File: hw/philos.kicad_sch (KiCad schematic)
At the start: 21 parts, among them SW1 Reset Button, U1 8086_Min_Mode, U10 MAX232N, U11 W27C512-45Z, U12 71256SA25TPGI, U2 SN74LS373N, U3 SN74LS373N, U4 SN74LS373N, U5 W27C512-45Z, U7 71256SA25TPGI, U8 SN74LS161AN, U9 SN74AHC14N, Y1 Crystal 15 MHz

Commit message: hw: add 8255 and 8259
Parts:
- added R4: 10K ohm, symbol Device:R
- added U13: 8259, Package_DIP:DIP-28_W15.24mm, symbol Interface:8259
- added U14: 8255, Package_DIP:DIP-40_W15.24mm, symbol Interface:8255
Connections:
- net GND: now also U13.14 (GND), U14.35 (RESET), U14.7 (GND); no longer U1.18 (INTR)
- net VCC: now also R4.2, U13.28 (VCC), U14.26 (VCC)
- net dati0: now also U13.11 (D0), U14.34 (D0)
- net dati1: now also U13.10 (D1), U14.33 (D1)
- net dati2: now also U13.9 (D2), U14.32 (D2)
- net dati3: now also U13.8 (D3), U14.31 (D3)
- net dati4: now also U13.7 (D4), U14.30 (D4)
- net dati5: now also U13.6 (D5), U14.29 (D5)
- net dati6: now also U13.5 (D6), U14.28 (D6)
- net dati7: now also U13.4 (D7), U14.27 (D7)
- net indirizzi18: now also U14.9 (A0)
- net indirizzi19: now also U13.27 (A0), U14.8 (A1)
- net at U1.32 (~{RD}), U12.22 (~{OE}), U6.13 (*RD)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: now also U13.3 (~{RD}), U14.5 (~{RD})
- net at U1.29 (~{WR}), U12.27 (~{WE}), U6.10 (*WR)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: now also U13.2 (~{WR}), U14.36 (~{WR})
- net at U1.24 (~{INTA}): now also U13.26 (~{INTA})
- new net: R4.1, U13.16 (~{SP}/~{EN})
- new net: U1.18 (INTR), U13.17 (INT)

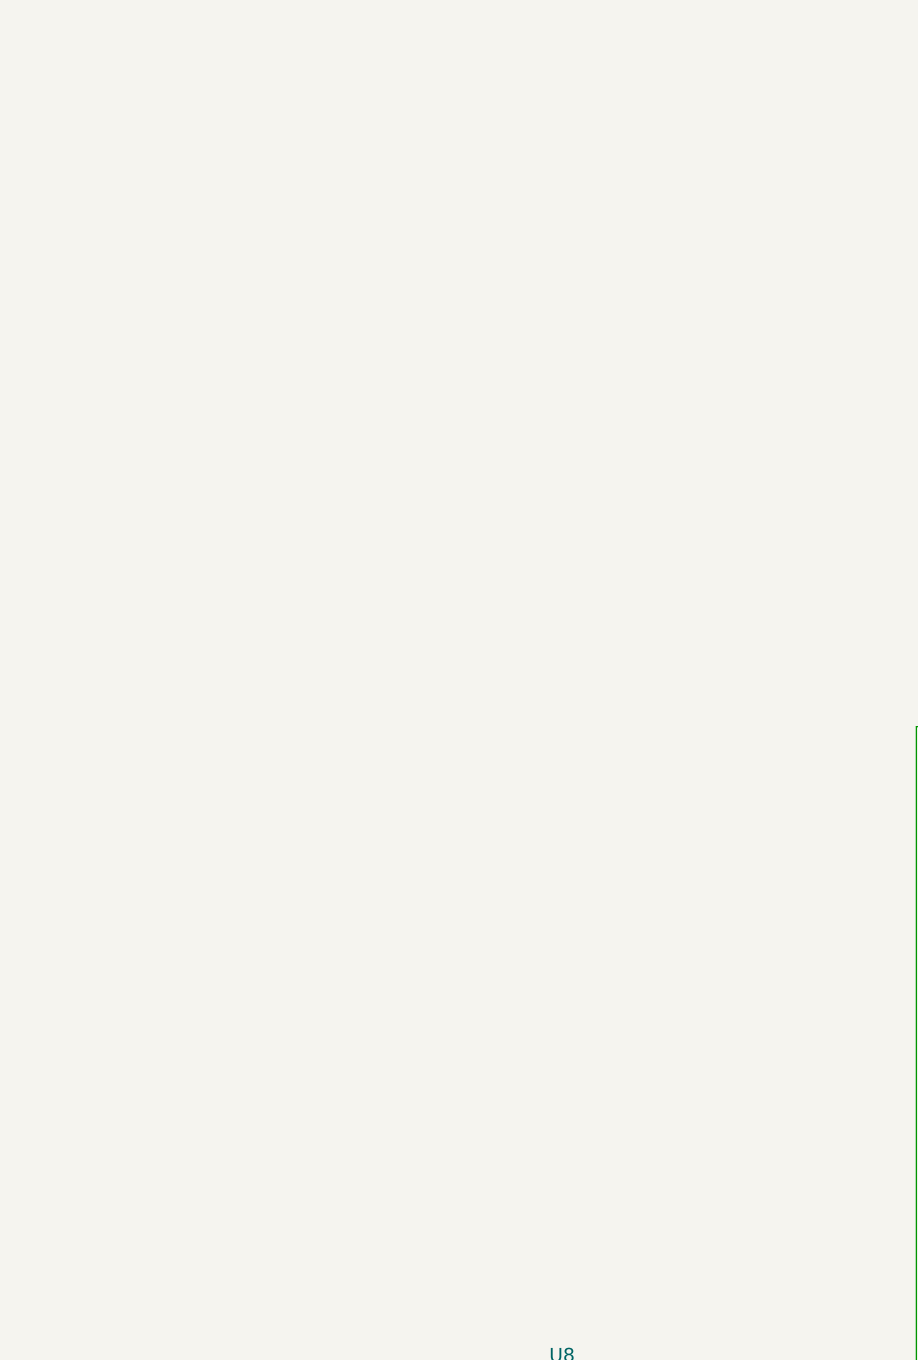
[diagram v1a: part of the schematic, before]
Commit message: hw: Add Arduino Mega
Signed-off-by: Matteo Bertolino <m.bertolino.m@gmail.com>
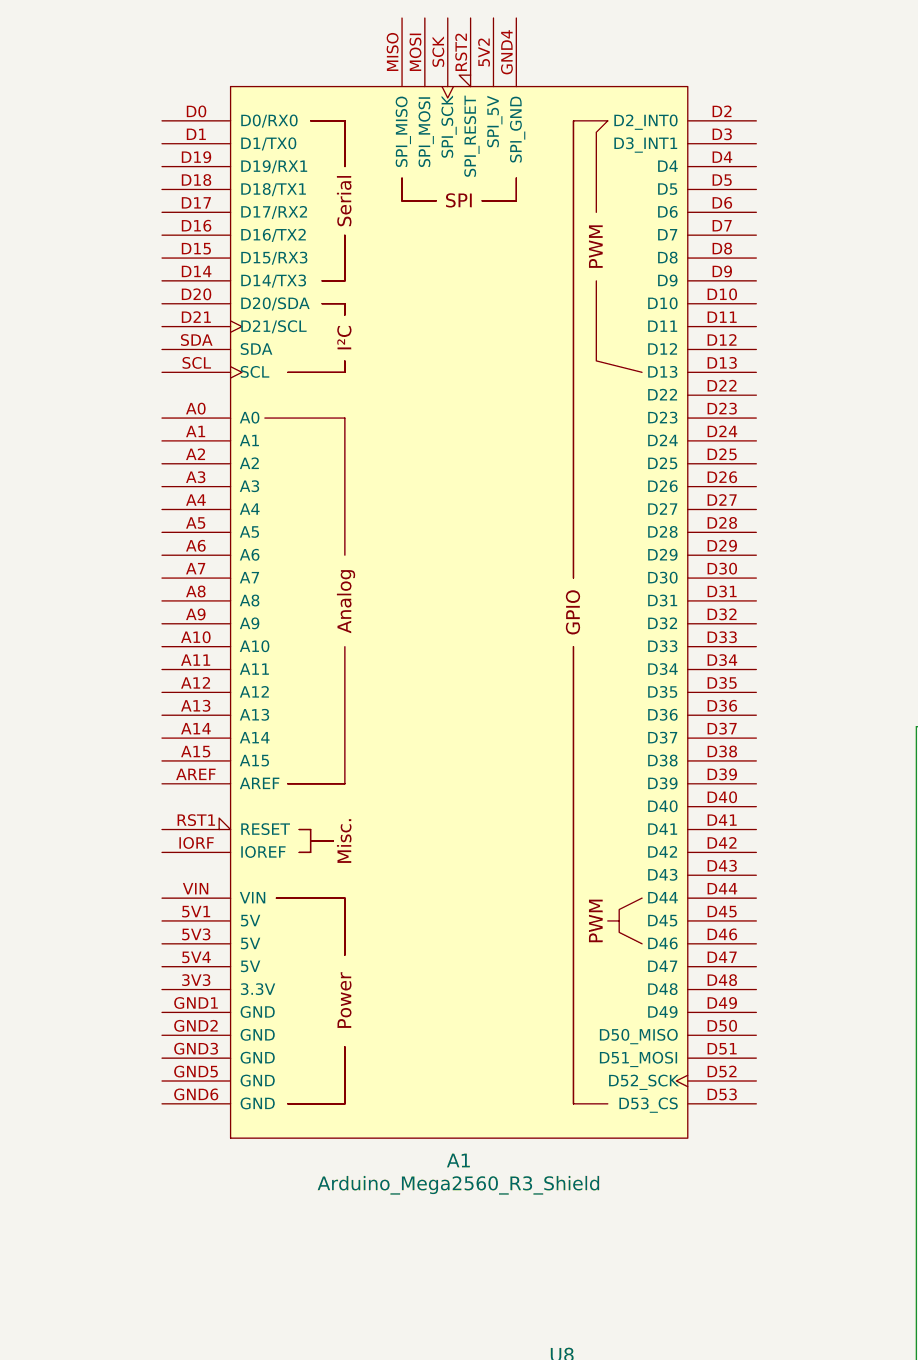
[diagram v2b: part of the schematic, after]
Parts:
- added A1: Arduino_Mega2560_R3_Shield, PCM_arduino-library:Arduino_Mega2560_R3_Shield, symbol Arduino:Arduino_Mega2560_R3_Shield

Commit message: docs: Add DFD prototype
Signed-off-by: Matteo Bertolino <m.bertolino.m@gmail.com>
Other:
- note added: "philOS"
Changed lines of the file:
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@@
 	(title_block
 		(title "philOS")
-		(date "2025-02-26")
+		(date "2025-03-07")
 		(rev "0")
 	)
+	(text "philOS"
+		(exclude_from_sim no)
+		(at 528.574 385.318 0)
+		(effects
+			(font
+				(face "Jersey 25")
+				(size 12 12)
+				(bold yes)
+				(color 0 0 0 1)
+			)
+		)
+	)
 	(junction
 		(at 92.71 200.66)
@@
 		)
 	)
-	(label "A19 1 = comando 0 = dato"
+	(label "A19: 1 = comando, 0 = dato"
 		(at 325.12 340.36 0)
 		(effects

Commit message: hw: manage the chip select pins
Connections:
- net indirizzi0: now also A1.D2 (D2_INT0)
- net indirizzi1: now also A1.D3 (D3_INT1)
- net indirizzi10: now also A1.D12
- net indirizzi11: now also A1.D13
- net indirizzi12: now also A1.D22
- net indirizzi13: now also A1.D23
- net indirizzi14: now also A1.D24
- net indirizzi15: now also A1.D25
- net indirizzi16: now also A1.D26
- net indirizzi17: now also A1.D27
- net indirizzi18: now also A1.D28
- net indirizzi19: now also A1.D29
- net indirizzi2: now also A1.D4
- net indirizzi3: now also A1.D5
- net indirizzi4: now also A1.D6
- net indirizzi5: now also A1.D7
- net indirizzi6: now also A1.D8
- net indirizzi7: now also A1.D9
- net indirizzi8: now also A1.D10
- net indirizzi9: now also A1.D11
- net at U5.20 (*CE): now also A1.D37
- net at U14.6 (~{CS}): now also A1.D33
- net at U7.20 (~{CS}): now also A1.D35, U12.20 (~{CS})
- net at U11.20 (*CE): now also A1.D36
- net at U1.28 (M/~{IO}): now also A1.D30
- net at DS1.8 (E): now also A1.D32
- net at A1.D31: now also U6.11 (*CS)
- net at A1.D34: now also U13.1 (~{CS})

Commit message: hw: improve the schematic
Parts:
- removed A1: Arduino_Mega2560_R3_Shield, PCM_arduino-library:Arduino_Mega2560_R3_Shield, symbol Arduino:Arduino_Mega2560_R3_Shield
- removed C1, C2: 15pF, K150J15C0GF5TL2_VIS, symbol K150J15C0GF5TL2:K150J15C0GF5TL2
- removed R1: 270 ohm, symbol Device:R
- removed R2: 1M ohm, symbol Device:R
- removed U10: MAX232N, N16, symbol MAX232N:MAX232N
- removed U11: W27C512-45Z, 28P-DIP, symbol W27C512-45Z:W27C512-45Z
- removed U12, U7: 71256SA25TPGI, 71256SA25TPGI:DIP787W47P254L3467H457Q28B, symbol 71256SA25TPGI:71256SA25TPGI
- removed U13: 8259, Package_DIP:DIP-28_W15.24mm, symbol Interface:8259
- removed U14: 8255, Package_DIP:DIP-40_W15.24mm, symbol Interface:8255
- removed U6: ~, symbol P8251A:P8251A
- removed U8: SN74LS161AN, N16, symbol SN74LS161AN:SN74LS161AN
- removed U9: SN74AHC14N, N14, symbol SN74AHC14N:SN74AHC14N
- removed Y1: Crystal 15 MHz, symbol Device:Crystal
- added A2: Arduino_Mega2560_R3_Shield, PCM_arduino-library:Arduino_Mega2560_R3_Shield, symbol Arduino:Arduino_Mega2560_R3_Shield
- added C3, C4: 15pF, K150J15C0GF5TL2_VIS, symbol K150J15C0GF5TL2:K150J15C0GF5TL2
- added R5: 10K ohm, symbol Device:R
- added R7: 270 ohm, symbol Device:R
- added U11, U16: 71256SA25TPGI, 71256SA25TPGI:DIP787W47P254L3467H457Q28B, symbol 71256SA25TPGI:71256SA25TPGI
- added U12: SN74LS161AN, N16, symbol SN74LS161AN:SN74LS161AN
- added U13: SN74AHC14N, N14, symbol SN74AHC14N:SN74AHC14N
- added U14: 8259, Package_DIP:DIP-28_W15.24mm, symbol Interface:8259
- added U15: W27C512-45Z, 28P-DIP, symbol W27C512-45Z:W27C512-45Z
- added U17: 8255, Package_DIP:DIP-40_W15.24mm, symbol Interface:8255
- added U18: MAX232N, N16, symbol MAX232N:MAX232N
- added U7: ~, symbol P8251A:P8251A
- added Y2: Crystal 15 MHz, symbol Device:Crystal
- R4: value 10K ohm -> 1M ohm
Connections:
- net GND: now also C3.2, C4.2, U11.14 (GND), U12.3 (A), U12.4 (B), U12.5 (C), U12.6 (D), U12.8 (GND), U13.7 (GND), U14.14 (GND), U15.14 (GND), U15.22 (*OE/VPP), U16.14 (GND), U17.35 (RESET), U17.7 (GND), U18.15 (GND), U18.2 (Vs+), U18.6 (Vs-), U7.17 (*CTS), U7.21 (reset), U7.22 (*DSR), U7.4 (GND)
- net VCC: now also R5.2, U11.28 (VCC), U12.1 (*CLR), U12.10 (ENT), U12.16 (VCC), U12.7 (ENP), U12.9 (*LOAD), U13.14 (VCC), U14.28 (VCC), U15.28 (VCC), U16.28 (VCC), U17.26 (VCC), U18.16 (VCC), U7.23 (*RTS), U7.26 (Vcc); no longer R4.2
- net dati0: now also U11.11 (I/O0), U14.11 (D0), U15.11 (Q0), U17.34 (D0), U7.27 (D0)
- net dati1: now also U11.12 (I/O1), U14.10 (D1), U15.12 (Q1), U17.33 (D1), U7.28 (D1)
- net dati10: now also U16.13 (I/O2)
- net dati11: now also U16.15 (I/O3)
- net dati12: now also U16.16 (I/O4)
- net dati13: now also U16.17 (I/O5)
- net dati14: now also U16.18 (I/O6)
- net dati15: now also U16.19 (I/O7)
- net dati2: now also U11.13 (I/O2), U14.9 (D2), U15.13 (Q2), U17.32 (D2), U7.1 (D2)
- net dati3: now also U11.15 (I/O3), U14.8 (D3), U15.15 (Q3), U17.31 (D3), U7.2 (D3)
- net dati4: now also U11.16 (I/O4), U14.7 (D4), U15.16 (Q4), U17.30 (D4), U7.5 (D4)
- net dati5: now also U11.17 (I/O5), U14.6 (D5), U15.17 (Q5), U17.29 (D5), U7.6 (D5)
- net dati6: now also U11.18 (I/O6), U14.5 (D6), U15.18 (Q6), U17.28 (D6), U7.7 (D6)
- net dati7: now also U11.19 (I/O7), U14.4 (D7), U15.19 (Q7), U17.27 (D7), U7.8 (D7)
- net dati8: now also U16.11 (I/O0)
- net dati9: now also U16.12 (I/O1)
- net indirizzi0: now also A2.D2 (D2_INT0), U11.10 (A0), U15.10 (A0), U16.10 (A0)
- net indirizzi1: now also A2.D3 (D3_INT1), U11.9 (A1), U15.9 (A1), U16.9 (A1)
- net indirizzi10: now also A2.D12, U11.21 (A10), U15.21 (A10), U16.21 (A10)
- net indirizzi11: now also A2.D13, U11.23 (A11), U15.23 (A11), U16.23 (A11)
- net indirizzi12: now also A2.D22, U11.2 (A12), U15.2 (A12), U16.2 (A12)
- net indirizzi13: now also A2.D23, U11.26 (A13), U15.26 (A13), U16.26 (A13)
- net indirizzi14: now also A2.D24, U11.1 (A14), U15.27 (A14), U16.1 (A14)
- net indirizzi15: now also A2.D25, U15.1 (A15)
- net indirizzi16: now also A2.D26
- net indirizzi17: now also A2.D27
- net indirizzi18: now also A2.D28, U17.9 (A0)
- net indirizzi19: now also A2.D29, U14.27 (A0), U17.8 (A1), U7.12 (C/*D)
- net indirizzi2: now also A2.D4, U11.8 (A2), U15.8 (A2), U16.8 (A2)
- net indirizzi3: now also A2.D5, U11.7 (A3), U15.7 (A3), U16.7 (A3)
- net indirizzi4: now also A2.D6, U11.6 (A4), U15.6 (A4), U16.6 (A4)
- net indirizzi5: now also A2.D7, U11.5 (A5), U15.5 (A5), U16.5 (A5)
- net indirizzi6: now also A2.D8, U11.4 (A6), U15.4 (A6), U16.4 (A6)
- net indirizzi7: now also A2.D9, U11.3 (A7), U15.3 (A7), U16.3 (A7)
- net indirizzi8: now also A2.D10, U11.25 (A8), U15.25 (A8), U16.25 (A8)
- net indirizzi9: now also A2.D11, U11.24 (A9), U15.24 (A9), U16.24 (A9)
- net at U5.20 (*CE): now also A2.D37
- net at U1.29 (~{WR}): now also U11.27 (~{WE}), U14.2 (~{WR}), U16.27 (~{WE}), U17.36 (~{WR}), U7.10 (*WR)
- net at U1.32 (~{RD}): now also U11.22 (~{OE}), U14.3 (~{RD}), U16.22 (~{OE}), U17.5 (~{RD}), U7.13 (*RD)
- net at U1.19 (CLK): now also U12.14 (QA)
- net at R4.1: now also C3.1, U13.1 (1A), Y2.1
- net at U1.18 (INTR): now also U14.17 (INT)
- net at U1.24 (~{INTA}): now also U14.26 (~{INTA})
- net at U1.28 (M/~{IO}): now also A2.D30
- net at DS1.8 (E): now also A2.D32
- new net: C4.1, R7.2, Y2.2
- new net: A2.D34, U14.1 (~{CS})
- new net: R5.1, U14.16 (~{SP}/~{EN})
- new net: U18.1 (C1+), U18.3 (C1-)
- new net: U18.11 (T1IN), U7.19 (TxD)
- new net: U18.12 (R1OUT), U7.3 (RxD)
- new net: U18.4 (C2+), U18.5 (C2-)
- new net: A2.D35, U11.20 (~{CS}), U16.20 (~{CS})
- new net: A2.D31, U7.11 (*CS)
- new net: A2.D33, U17.6 (~{CS})
- new net: A2.D36, U15.20 (*CE)
- new net: R4.2, R7.1, U12.2 (CLK), U13.2 (1Y)
- new net: U12.11 (QD), U7.20 (CLK)
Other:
- moved on the sheet: DS1, R3, R6, SW1, U1, U2, U3, U4, U5

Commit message: hw: improved the schematic again
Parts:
- removed DS1: HY1602E, Display:HY1602E, symbol Display_Character:HY1602E
- removed R3, R6: 1K ohm, symbol Device:R
- removed SW1: Reset Button, symbol Switch:SW_Push
- removed U2, U3, U4: SN74LS373N, N20, symbol SN74LS373N:SN74LS373N
- added DS2: HY1602E, Display:HY1602E, symbol Display_Character:HY1602E
- added R8, R9: 1K ohm, symbol Device:R
- added SW2: Reset Button, symbol Switch:SW_Push
- added U6, U8, U9: SN74LS373N, N20, symbol SN74LS373N:SN74LS373N
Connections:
- net GND: now also DS2.1 (LEDK), DS2.3 (VSS), DS2.7 (R/~{W}), SW2.2, U6.1 (*OC), U6.10 (GND), U8.1 (*OC), U8.10 (GND), U9.1 (*OC), U9.10 (GND)
- net VCC: now also DS2.2 (LEDA), DS2.4 (VDD), R8.2, R9.1, U6.20 (VCC), U8.20 (VCC), U9.20 (VCC)
- net dati0: now also DS2.9 (DB0), U6.3 (1D)
- net dati1: now also DS2.10 (DB1), U6.4 (2D)
- net dati10: now also U8.7 (3D)
- net dati11: now also U8.8 (4D)
- net dati12: now also U8.18 (8D)
- net dati13: now also U8.17 (7D)
- net dati14: now also U8.14 (6D)
- net dati15: now also U8.13 (5D)
- net dati2: now also DS2.11 (DB2), U6.7 (3D)
- net dati3: now also DS2.12 (DB3), U6.8 (4D)
- net dati4: now also DS2.13 (DB4), U6.18 (8D)
- net dati5: now also DS2.14 (DB5), U6.17 (7D)
- net dati6: now also DS2.15 (DB6), U6.14 (6D)
- net dati7: now also DS2.16 (DB7), U6.13 (5D)
- net dati8: now also U8.3 (1D)
- net dati9: now also U8.4 (2D)
- net indirizzi0: now also U6.2 (1Q)
- net indirizzi1: now also U6.5 (2Q)
- net indirizzi10: now also U8.6 (3Q)
- net indirizzi11: now also U8.9 (4Q)
- net indirizzi12: now also U8.19 (8Q)
- net indirizzi13: now also U8.16 (7Q)
- net indirizzi14: now also U8.15 (6Q)
- net indirizzi15: now also U8.12 (5Q)
- net indirizzi16: now also U9.2 (1Q)
- net indirizzi17: now also U9.5 (2Q)
- net indirizzi18: now also U9.6 (3Q)
- net indirizzi19: now also DS2.6 (RS), U9.9 (4Q)
- net indirizzi2: now also U6.6 (3Q)
- net indirizzi3: now also U6.9 (4Q)
- net indirizzi4: now also U6.19 (8Q)
- net indirizzi5: now also U6.16 (7Q)
- net indirizzi6: now also U6.15 (6Q)
- net indirizzi7: now also U6.12 (5Q)
- net indirizzi8: now also U8.2 (1Q)
- net indirizzi9: now also U8.5 (2Q)
- net at A2.D32: now also DS2.8 (E)
- net at U1.25 (ALE): now also U6.11 (LE), U8.11 (LE), U9.11 (LE)
- net at U1.35 (A19/S6): now also U9.8 (4D)
- net at U1.36 (A18/S5): now also U9.7 (3D)
- net at U1.37 (A17/S4): now also U9.4 (2D)
- net at U1.38 (A16/S3): now also U9.3 (1D)
- new net: R8.1, SW2.1
- new net: DS2.5 (Vo), R9.2
